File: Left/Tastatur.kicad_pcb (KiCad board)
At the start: 2 copper layers, 125.5 x 85.1 mm, 145 parts, among them J102 Conn_01x04_Pin, J103 XT60PW-M, Q101 SI2301CDS-T1-GE3, Q102 SI2301CDS-T1-GE3, Q103 SI2301CDS-T1-GE3, Q104 SI2301CDS-T1-GE3, Q105 SI2301CDS-T1-GE3, Q106 2N7002HW, Q107 SI2301CDS-T1-GE3, SW201 SW_Push, SW202 SW_Push, SW203 SW_Push, SW204 SW_Push, SW205 SW_Push, SW206 SW_Push, SW207 SW_Push, SW208 SW_Push, SW209 SW_Push, SW210 SW_Push, SW211 SW_Push, SW212 SW_Push, SW213 SW_Push, SW214 SW_Push, SW215 SW_Push, SW216 SW_Push, SW217 SW_Push, SW218 SW_Push, SW219 SW_Push, SW221 MK-12C02-G020, U101 USBLC6-2SC6, U102 CH592F, U103 AP2112K-3.3, U104 MT3608, U105 TP4056-42-ESOP8, U106 CD4052B, U107 LM393, Y101 32MHz

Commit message: update
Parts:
- moved H201 13.8 mm to (80.9, 132.4)
- moved H202 0.55 mm to (174.8, 90.4)
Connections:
- AE101 pad 2: GNDS -> GND
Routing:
- net GND: track 111.4 -> 115.9 mm, vias 34 -> 36
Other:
- board size 125.5 x 85.1 mm -> 125 x 85 mm

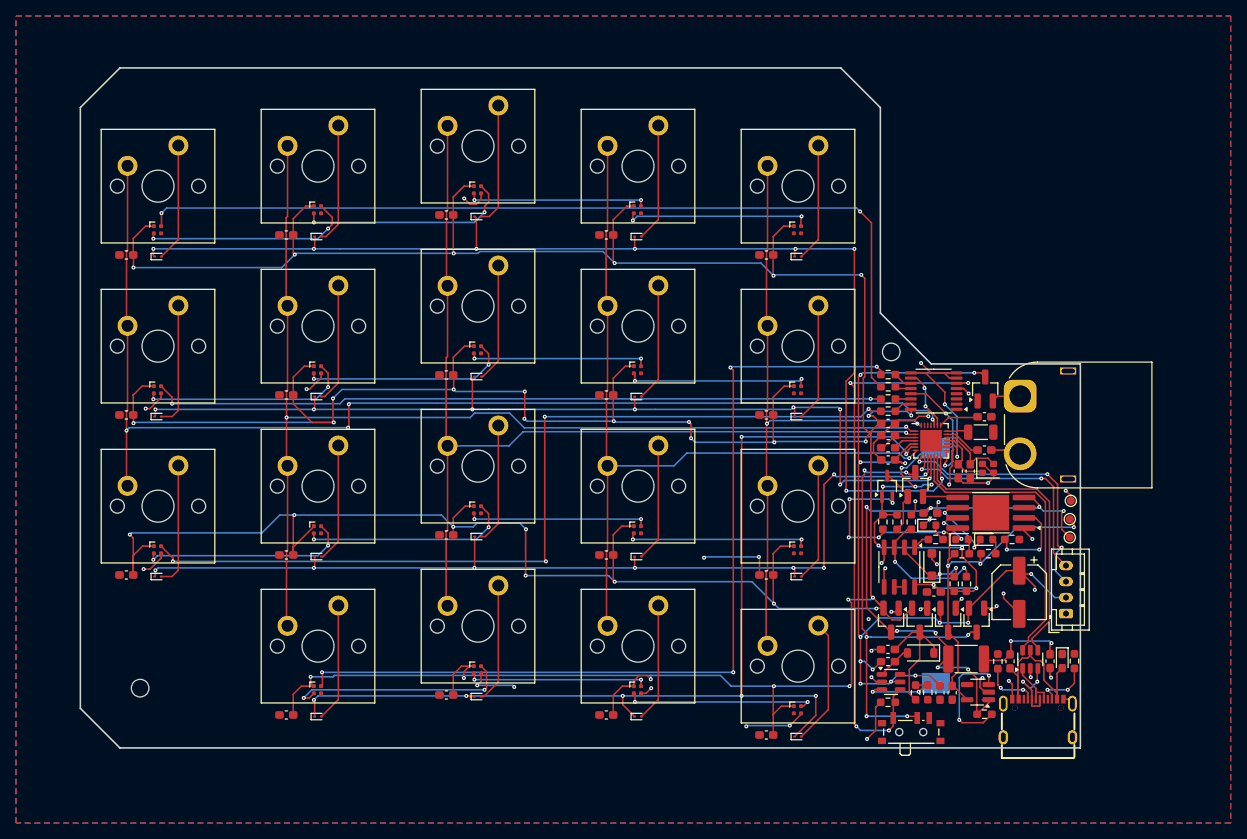
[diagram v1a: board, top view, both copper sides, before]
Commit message: redesign with smaller components
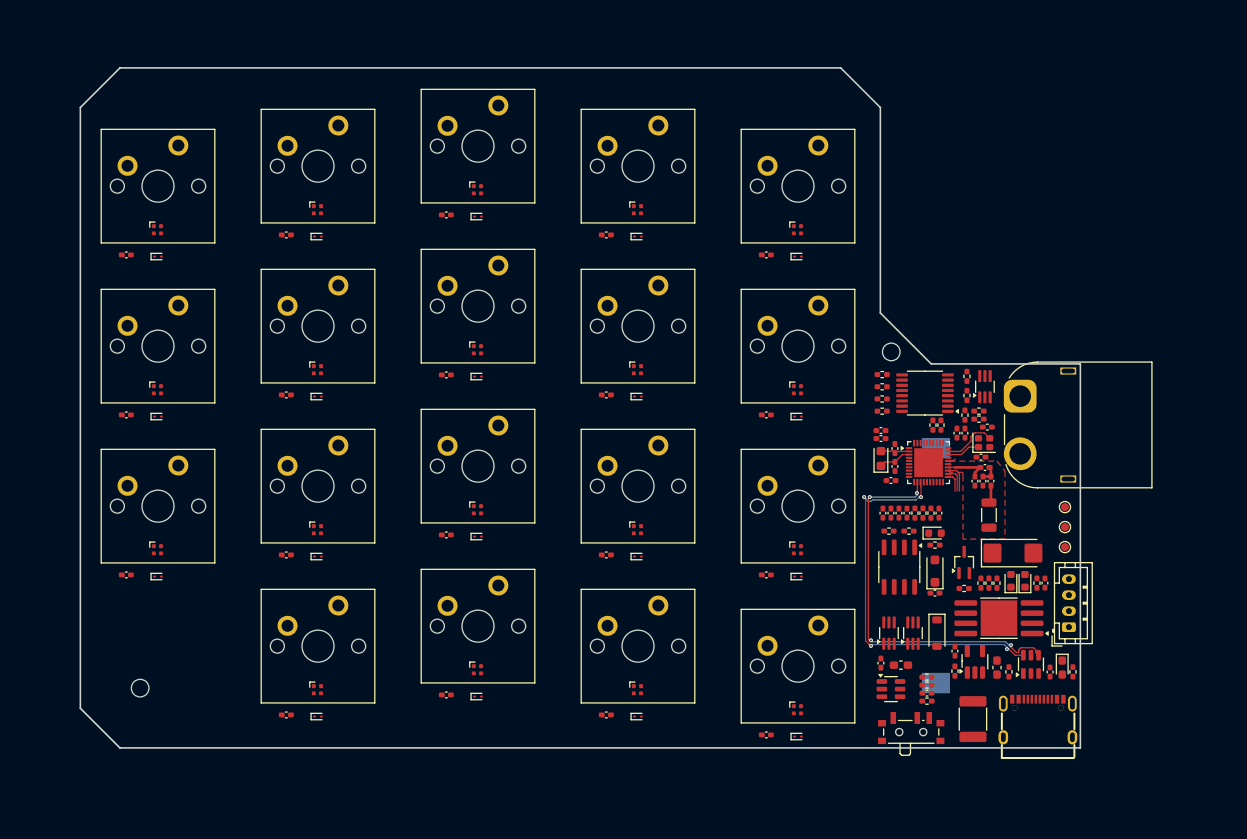
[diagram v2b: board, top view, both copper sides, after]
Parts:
- removed AE101: Antenna_Shield, Inductor_SMD:L_1206_3216Metric
- removed C101: 470n, Capacitor_SMD:C_0603_1608Metric_Pad1.08x0.95mm_HandSolder
- removed C102: 4u7, Capacitor_SMD:C_0603_1608Metric_Pad1.08x0.95mm_HandSolder
- removed C103: 100n, Capacitor_SMD:C_0603_1608Metric_Pad1.08x0.95mm_HandSolder
- removed C104: 2u2, Capacitor_SMD:C_0603_1608Metric_Pad1.08x0.95mm_HandSolder
- removed C105, C106: 10p, Capacitor_SMD:C_0603_1608Metric_Pad1.08x0.95mm_HandSolder
- removed J102: Conn_01x04_Pin, Connector_JST:JST_PH_B4B-PH-K_1x04_P2.00mm_Vertical
- removed L101: 10u, Inductor_SMD:L_0603_1608Metric_Pad1.05x0.95mm_HandSolder
- removed Q101, Q102, Q103, Q104, Q105, Q107: SI2301CDS-T1-GE3, Package_TO_SOT_SMD:SOT-23_Handsoldering
- removed U102: CH592F, steew:CH592F
- removed Y101: 32MHz, Crystal:Crystal_SMD_2016-4Pin_2.0x1.6mm
- added AE1: Antenna_Shield, Inductor_SMD:L_1206_3216Metric, F.Cu at (187.0, 110.8)
- added C1: 4u7, Capacitor_SMD:C_0402_1005Metric_Pad0.74x0.62mm_HandSolder, F.Cu at (174.8, 106.4)
- added C2: 1u, Capacitor_SMD:C_0402_1005Metric_Pad0.74x0.62mm_HandSolder, F.Cu at (183.0, 100.5)
- added C3: 100p, Capacitor_SMD:C_0402_1005Metric_Pad0.74x0.62mm_HandSolder, F.Cu at (184.0, 100.5)
- added C35: 1p, Capacitor_SMD:C_0402_1005Metric_Pad0.74x0.62mm_HandSolder, F.Cu at (185.2, 106.5)
- added C36: 802p, Capacitor_SMD:C_0402_1005Metric_Pad0.74x0.62mm_HandSolder, F.Cu at (180.8, 110.5)
- added C37: 4u7, Capacitor_SMD:C_0402_1005Metric_Pad0.74x0.62mm_HandSolder, F.Cu at (175.8, 110.5)
- added C38: 4u7, Capacitor_SMD:C_0402_1005Metric_Pad0.74x0.62mm_HandSolder, F.Cu at (173.8, 110.5)
- added C39: 4u7, Capacitor_SMD:C_0402_1005Metric_Pad0.74x0.62mm_HandSolder, F.Cu at (174.8, 110.5)
- added C4: 100n, Capacitor_SMD:C_0402_1005Metric_Pad0.74x0.62mm_HandSolder, F.Cu at (176.8, 110.5)
- added C40: 1p2, Capacitor_SMD:C_0402_1005Metric_Pad0.74x0.62mm_HandSolder, F.Cu at (186.2, 106.5)
- added C41: 12p, Capacitor_SMD:C_0402_1005Metric_Pad0.74x0.62mm_HandSolder, F.Cu at (175.2, 102.4)
- added C42: 12p, Capacitor_SMD:C_0402_1005Metric_Pad0.74x0.62mm_HandSolder, F.Cu at (175.2, 104.7)
- added C5: 100n, Capacitor_SMD:C_0402_1005Metric_Pad0.74x0.62mm_HandSolder, F.Cu at (173.5, 101.2)
- added C6: 10p, Capacitor_SMD:C_0402_1005Metric_Pad0.74x0.62mm_HandSolder, F.Cu at (186.0, 103.5)
- added C9: 10p, Capacitor_SMD:C_0402_1005Metric_Pad0.74x0.62mm_HandSolder, F.Cu at (186.8, 99.8)
- added J1: Conn_01x04_Pin, Connector_JST:JST_PH_B4B-PH-K_1x04_P2.00mm_Vertical, F.Cu at (197.0, 124.8)
- added L3: 4n7, Inductor_SMD:L_0402_1005Metric_Pad0.77x0.64mm_HandSolder, F.Cu at (186.5, 104.8)
- added L4: 2n2, Inductor_SMD:L_0402_1005Metric_Pad0.77x0.64mm_HandSolder, F.Cu at (187.2, 106.5)
- added Q1: NTJD4152PT1G, Package_TO_SOT_SMD:SOT-363_SC-70-6_Handsoldering, F.Cu at (174.5, 125.5)
- added Q2: NTJD4152PT1G, Package_TO_SOT_SMD:SOT-363_SC-70-6_Handsoldering, F.Cu at (186.5, 94.7)
- added Q8: NTJD4152PT1G, Package_TO_SOT_SMD:SOT-363_SC-70-6_Handsoldering, F.Cu at (177.5, 125.5)
- added R1: 100R, Resistor_SMD:R_0402_1005Metric_Pad0.72x0.64mm_HandSolder, F.Cu at (179.8, 110.5)
- added R16: 4K7, Resistor_SMD:R_0402_1005Metric_Pad0.72x0.64mm_HandSolder, F.Cu at (185.8, 98.8)
- added R18: 4K7, Resistor_SMD:R_0402_1005Metric_Pad0.72x0.64mm_HandSolder, F.Cu at (184.2, 93.4)
- added R19: 4K7, Resistor_SMD:R_0402_1005Metric_Pad0.72x0.64mm_HandSolder, F.Cu at (184.2, 95.8)
- added R20: 4K7, Resistor_SMD:R_0402_1005Metric_Pad0.72x0.64mm_HandSolder, F.Cu at (184.0, 98.2)
- added R25: 100R, Resistor_SMD:R_0402_1005Metric_Pad0.72x0.64mm_HandSolder, F.Cu at (178.8, 110.5)
- added R26: 4k7, Resistor_SMD:R_0402_1005Metric_Pad0.72x0.64mm_HandSolder, F.Cu at (177.8, 110.5)
- added R28: 0R, Resistor_SMD:R_0402_1005Metric_Pad0.72x0.64mm_HandSolder, F.Cu at (180.0, 99.5)
- added R29: 0R, Resistor_SMD:R_0402_1005Metric_Pad0.72x0.64mm_HandSolder, F.Cu at (181.0, 99.5)
- added U8: nRF52833_QDxx, Package_DFN_QFN:QFN-40-1EP_5x5mm_P0.4mm_EP3.6x3.6mm, F.Cu at (179.4, 104.2)
- added Y1: 32MHz, Crystal:Crystal_SMD_2016-4Pin_2.0x1.6mm, F.Cu at (186.4, 101.7)
- added Y2: 32768 KHz, Crystal:Crystal_SMD_2012-2Pin_2.0x1.2mm_HandSoldering, F.Cu at (173.5, 103.7)
- C10: renamed from C109; footprint Capacitor_SMD:C_0603_1608Metric_Pad1.08x0.95mm_HandSolder -> Capacitor_SMD:C_0402_1005Metric_Pad0.74x0.62mm_HandSolder
- C11: renamed from C110; footprint Capacitor_SMD:C_0603_1608Metric_Pad1.08x0.95mm_HandSolder -> Capacitor_SMD:C_0402_1005Metric_Pad0.74x0.62mm_HandSolder
- C12: renamed from C111; footprint Capacitor_SMD:C_0603_1608Metric_Pad1.08x0.95mm_HandSolder -> Capacitor_SMD:C_0402_1005Metric_Pad0.74x0.62mm_HandSolder
- C13: renamed from C112; footprint Capacitor_SMD:CP_Elec_6.3x7.7 -> Capacitor_Tantalum_SMD:CP_EIA-6032-28_Kemet-C_HandSolder
- C14: renamed from C113; footprint Capacitor_SMD:C_0603_1608Metric_Pad1.08x0.95mm_HandSolder -> Capacitor_SMD:C_0402_1005Metric_Pad0.74x0.62mm_HandSolder
- C15: renamed from C114; footprint Capacitor_SMD:C_0603_1608Metric_Pad1.08x0.95mm_HandSolder -> Capacitor_SMD:C_0402_1005Metric_Pad0.74x0.62mm_HandSolder
- C16: renamed from C201; footprint Capacitor_SMD:C_0603_1608Metric_Pad1.08x0.95mm_HandSolder -> Capacitor_SMD:C_0402_1005Metric_Pad0.74x0.62mm_HandSolder
- C17: renamed from C202; footprint Capacitor_SMD:C_0603_1608Metric_Pad1.08x0.95mm_HandSolder -> Capacitor_SMD:C_0402_1005Metric_Pad0.74x0.62mm_HandSolder
- C18: renamed from C203; footprint Capacitor_SMD:C_0603_1608Metric_Pad1.08x0.95mm_HandSolder -> Capacitor_SMD:C_0402_1005Metric_Pad0.74x0.62mm_HandSolder
- C19: renamed from C204; footprint Capacitor_SMD:C_0603_1608Metric_Pad1.08x0.95mm_HandSolder -> Capacitor_SMD:C_0402_1005Metric_Pad0.74x0.62mm_HandSolder
- C20: renamed from C205; footprint Capacitor_SMD:C_0603_1608Metric_Pad1.08x0.95mm_HandSolder -> Capacitor_SMD:C_0402_1005Metric_Pad0.74x0.62mm_HandSolder
- C21: renamed from C206; footprint Capacitor_SMD:C_0603_1608Metric_Pad1.08x0.95mm_HandSolder -> Capacitor_SMD:C_0402_1005Metric_Pad0.74x0.62mm_HandSolder
- C22: renamed from C207; footprint Capacitor_SMD:C_0603_1608Metric_Pad1.08x0.95mm_HandSolder -> Capacitor_SMD:C_0402_1005Metric_Pad0.74x0.62mm_HandSolder
- C23: renamed from C208; footprint Capacitor_SMD:C_0603_1608Metric_Pad1.08x0.95mm_HandSolder -> Capacitor_SMD:C_0402_1005Metric_Pad0.74x0.62mm_HandSolder
- C24: renamed from C209; footprint Capacitor_SMD:C_0603_1608Metric_Pad1.08x0.95mm_HandSolder -> Capacitor_SMD:C_0402_1005Metric_Pad0.74x0.62mm_HandSolder
- C25: renamed from C210; footprint Capacitor_SMD:C_0603_1608Metric_Pad1.08x0.95mm_HandSolder -> Capacitor_SMD:C_0402_1005Metric_Pad0.74x0.62mm_HandSolder
- C26: renamed from C211; footprint Capacitor_SMD:C_0603_1608Metric_Pad1.08x0.95mm_HandSolder -> Capacitor_SMD:C_0402_1005Metric_Pad0.74x0.62mm_HandSolder
- C27: renamed from C212; footprint Capacitor_SMD:C_0603_1608Metric_Pad1.08x0.95mm_HandSolder -> Capacitor_SMD:C_0402_1005Metric_Pad0.74x0.62mm_HandSolder
- C28: renamed from C213; footprint Capacitor_SMD:C_0603_1608Metric_Pad1.08x0.95mm_HandSolder -> Capacitor_SMD:C_0402_1005Metric_Pad0.74x0.62mm_HandSolder
- C29: renamed from C214; footprint Capacitor_SMD:C_0603_1608Metric_Pad1.08x0.95mm_HandSolder -> Capacitor_SMD:C_0402_1005Metric_Pad0.74x0.62mm_HandSolder
- C30: renamed from C215; footprint Capacitor_SMD:C_0603_1608Metric_Pad1.08x0.95mm_HandSolder -> Capacitor_SMD:C_0402_1005Metric_Pad0.74x0.62mm_HandSolder
- C31: renamed from C216; footprint Capacitor_SMD:C_0603_1608Metric_Pad1.08x0.95mm_HandSolder -> Capacitor_SMD:C_0402_1005Metric_Pad0.74x0.62mm_HandSolder
- C32: renamed from C217; footprint Capacitor_SMD:C_0603_1608Metric_Pad1.08x0.95mm_HandSolder -> Capacitor_SMD:C_0402_1005Metric_Pad0.74x0.62mm_HandSolder
- C33: renamed from C218; footprint Capacitor_SMD:C_0603_1608Metric_Pad1.08x0.95mm_HandSolder -> Capacitor_SMD:C_0402_1005Metric_Pad0.74x0.62mm_HandSolder
- C34: renamed from C219; footprint Capacitor_SMD:C_0603_1608Metric_Pad1.08x0.95mm_HandSolder -> Capacitor_SMD:C_0402_1005Metric_Pad0.74x0.62mm_HandSolder
- C7: renamed from C107; footprint Capacitor_SMD:C_0603_1608Metric_Pad1.08x0.95mm_HandSolder -> Capacitor_SMD:C_0402_1005Metric_Pad0.74x0.62mm_HandSolder
- C8: renamed from C108; footprint Capacitor_SMD:C_0603_1608Metric_Pad1.08x0.95mm_HandSolder -> Capacitor_SMD:C_0402_1005Metric_Pad0.74x0.62mm_HandSolder
- R10: renamed from R108; footprint Resistor_SMD:R_0603_1608Metric_Pad0.98x0.95mm_HandSolder -> Resistor_SMD:R_0402_1005Metric_Pad0.72x0.64mm_HandSolder
- R11: renamed from R109; footprint Resistor_SMD:R_0603_1608Metric_Pad0.98x0.95mm_HandSolder -> Resistor_SMD:R_0402_1005Metric_Pad0.72x0.64mm_HandSolder
- R12: renamed from R110; footprint Resistor_SMD:R_0603_1608Metric_Pad0.98x0.95mm_HandSolder -> Resistor_SMD:R_0402_1005Metric_Pad0.72x0.64mm_HandSolder
- R13: renamed from R111; footprint Resistor_SMD:R_0603_1608Metric_Pad0.98x0.95mm_HandSolder -> Resistor_SMD:R_0402_1005Metric_Pad0.72x0.64mm_HandSolder
- R14: renamed from R112; footprint Resistor_SMD:R_0603_1608Metric_Pad0.98x0.95mm_HandSolder -> Resistor_SMD:R_0402_1005Metric_Pad0.72x0.64mm_HandSolder
- R15: renamed from R113; footprint Resistor_SMD:R_0603_1608Metric_Pad0.98x0.95mm_HandSolder -> Resistor_SMD:R_0402_1005Metric_Pad0.72x0.64mm_HandSolder
- R17: renamed from R114; footprint Resistor_SMD:R_0603_1608Metric_Pad0.98x0.95mm_HandSolder -> Resistor_SMD:R_0402_1005Metric_Pad0.72x0.64mm_HandSolder
- R2: renamed from R205; footprint Resistor_SMD:R_0603_1608Metric_Pad0.98x0.95mm_HandSolder -> Resistor_SMD:R_0402_1005Metric_Pad0.72x0.64mm_HandSolder
- R21: renamed from R201; footprint Resistor_SMD:R_0603_1608Metric_Pad0.98x0.95mm_HandSolder -> Resistor_SMD:R_0402_1005Metric_Pad0.72x0.64mm_HandSolder
- R22: renamed from R202; footprint Resistor_SMD:R_0603_1608Metric_Pad0.98x0.95mm_HandSolder -> Resistor_SMD:R_0402_1005Metric_Pad0.72x0.64mm_HandSolder
- R23: renamed from R203; footprint Resistor_SMD:R_0603_1608Metric_Pad0.98x0.95mm_HandSolder -> Resistor_SMD:R_0402_1005Metric_Pad0.72x0.64mm_HandSolder
- R24: renamed from R204; footprint Resistor_SMD:R_0603_1608Metric_Pad0.98x0.95mm_HandSolder -> Resistor_SMD:R_0402_1005Metric_Pad0.72x0.64mm_HandSolder
- R3: renamed from R101; footprint Resistor_SMD:R_0603_1608Metric_Pad0.98x0.95mm_HandSolder -> Resistor_SMD:R_0402_1005Metric_Pad0.72x0.64mm_HandSolder
- R4: renamed from R102; footprint Resistor_SMD:R_0603_1608Metric_Pad0.98x0.95mm_HandSolder -> Resistor_SMD:R_0402_1005Metric_Pad0.72x0.64mm_HandSolder
- R5: renamed from R103; footprint Resistor_SMD:R_0603_1608Metric_Pad0.98x0.95mm_HandSolder -> Resistor_SMD:R_0402_1005Metric_Pad0.72x0.64mm_HandSolder
- R6: renamed from R104; footprint Resistor_SMD:R_0603_1608Metric_Pad0.98x0.95mm_HandSolder -> Resistor_SMD:R_0402_1005Metric_Pad0.72x0.64mm_HandSolder
- R7: renamed from R105; footprint Resistor_SMD:R_0603_1608Metric_Pad0.98x0.95mm_HandSolder -> Resistor_SMD:R_0402_1005Metric_Pad0.72x0.64mm_HandSolder
- R8: renamed from R106; footprint Resistor_SMD:R_0603_1608Metric_Pad0.98x0.95mm_HandSolder -> Resistor_SMD:R_0402_1005Metric_Pad0.72x0.64mm_HandSolder
- R9: renamed from R107; footprint Resistor_SMD:R_0603_1608Metric_Pad0.98x0.95mm_HandSolder -> Resistor_SMD:R_0402_1005Metric_Pad0.72x0.64mm_HandSolder
- moved R10 17.2 mm to (185.8, 97.8), turned to 180 degrees
- moved C12 16.8 mm to (194.0, 119.2), turned to -90 degrees
- moved R12 14.4 mm to (186.0, 119.2), turned to 90 degrees
- moved Q6 13.5 mm to (183.9, 116.7)
- moved U5 13.2 mm to (188.2, 123.6)
- moved R13 11.7 mm to (174.5, 112.8), turned to 0 degrees
- moved D4 9.43 mm to (191.5, 119.0), turned to 90 degrees
- moved F1 7.55 mm to (185.0, 136.2), turned to -90 degrees
- moved R5 6.53 mm to (182.8, 130.2), turned to 90 degrees
- moved R11 6.28 mm to (193.0, 119.2), turned to 90 degrees
- moved D3 6.01 mm to (189.8, 119.0), turned to 90 degrees
- moved R9 5.72 mm to (188.0, 119.2), turned to 90 degrees
- moved C11 5.23 mm to (182.8, 127.8)
- moved C13 4.96 mm to (190.0, 115.5), turned to 0 degrees
- moved R2 4.87 mm to (179.2, 134.0), turned to 0 degrees
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- renumbered BT101 to BT1, D101 to D1, D254 to D10, D255 to D11, D201 to D12, D202 to D13, D203 to D14, D204 to D15, D205 to D16, D256 to D17, D257 to D18, D258 to D19, D102 to D2, D259 to D20, D260 to D21, D206 to D22, D207 to D23, D208 to D24, D209 to D25, D210 to D26, D261 to D27, D262 to D28, D263 to D29, D103 to D3, D264 to D30, D265 to D31, D211 to D32, D212 to D33, D213 to D34, D214 to D35, D215 to D36, D266 to D37, D267 to D38, D268 to D39, D104 to D4, D269 to D40, D216 to D41, D217 to D42, D218 to D43, D219 to D44, D105 to D5, D106 to D6, D251 to D7, D252 to D8, D253 to D9, F101 to F1, H201 to H1, H202 to H2, J103 to J3, L102 to L1, L103 to L2, Q106 to Q6, SW221 to SW1, SW209 to SW10, SW210 to SW11, SW211 to SW12, SW212 to SW13, SW213 to SW14, SW214 to SW15, SW215 to SW16, SW216 to SW17, SW217 to SW18, SW218 to SW19, SW201 to SW2, SW219 to SW20, SW202 to SW3, SW203 to SW4, SW204 to SW5, SW205 to SW6, SW206 to SW7, SW207 to SW8, SW208 to SW9, TP101 to TP1, TP103 to TP2, TP104 to TP3, U101 to U1, U103 to U3, U104 to U4, U105 to U5, U106 to U6, U107 to U7, USB101 to USB1
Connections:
- SW1 pad 2: +3V3BAT -> +3V3
- U6 pad 1: GND -> Net-(U6-Y0)
- U6 pad 2: GND -> Net-(U6-Y2)
- U6 pad 4: GND -> Net-(U6-Y3)
- U6 pad 5: GND -> Net-(U6-Y1)
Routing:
- net +5V: track 603.9 -> 0.00 mm, vias 34 -> 0
- net /COL0: track 146.1 -> 0.00 mm, vias 4 -> 0
- net /ROW0: track 143.3 -> 0.00 mm, vias 8 -> 0
- net /COL1: track 140.3 -> 0.00 mm, vias 2 -> 0
- net /ROW3: track 131.2 -> 0.00 mm, vias 7 -> 0
- net /COL2: track 119.8 -> 0.00 mm, vias 1 -> 0
- net /ROW1: track 119.2 -> 0.00 mm, vias 8 -> 0
- net /ROW2: track 118.7 -> 0.00 mm, vias 8 -> 0
- net +3V3: track 118.0 -> 0.00 mm, vias 14 -> 0
- net GND: track 115.9 -> 0.00 mm, vias 36 -> 0
- net Net-(D7-DIN): track 112.4 -> 0.00 mm, vias 2 -> 0
- net Net-(D37-DIN): track 111.0 -> 0.00 mm, vias 4 -> 0
- net Net-(D27-DIN): track 109.8 -> 0.00 mm, vias 4 -> 0
- net /COL3: track 100.3 -> 0.00 mm, vias 1 -> 0
- net Net-(D17-DIN): track 91.6 -> 0.00 mm, vias 2 -> 0
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- removed copper zone on B.Cu, net GND
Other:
- board text added: "0"
- board text added: "0 mm"
- board text added: "0.01 mm"
- board text added: "0.02"
- board text added: "0.035 mm"
- board text added: "1"
- board text added: "1.51 mm"
- board text added: "3.3"
- board text added: "4.5"
- board text added: "B.Cu"
- board text added: "B.Mask"
- board text added: "B.Paste"
- board text added: "B.Silkscreen"
- board text added: "Bottom Silk Screen"
- board text added: "Bottom Solder Mask"
- board text added: "Bottom Solder Paste"
- board text added: "Color"
- board text added: "Dielectric 1"
- board text added: "Epsilon R"
- board text added: "F.Cu"
- board text added: "F.Mask"
- board text added: "F.Paste"
- board text added: "F.Silkscreen"
- board text added: "FR4"
- board text added: "Layer Name"
- board text added: "Loss Tangent"
- board text added: "Material"
- board text added: "Not specified"
- board text added: "Thickness (mm)"
- board text added: "Top Silk Screen"
- board text added: "Top Solder Mask"
- board text added: "Top Solder Paste"
- board text added: "Type"
- board text added: "copper"
- board text added: "core"
